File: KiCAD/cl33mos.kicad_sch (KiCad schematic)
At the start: 13 parts, among them J1 USB_B_Micro, J2 Edge2x6_Connector, U2 ESP32-WROOM-32, U3 AMS1117-3.3

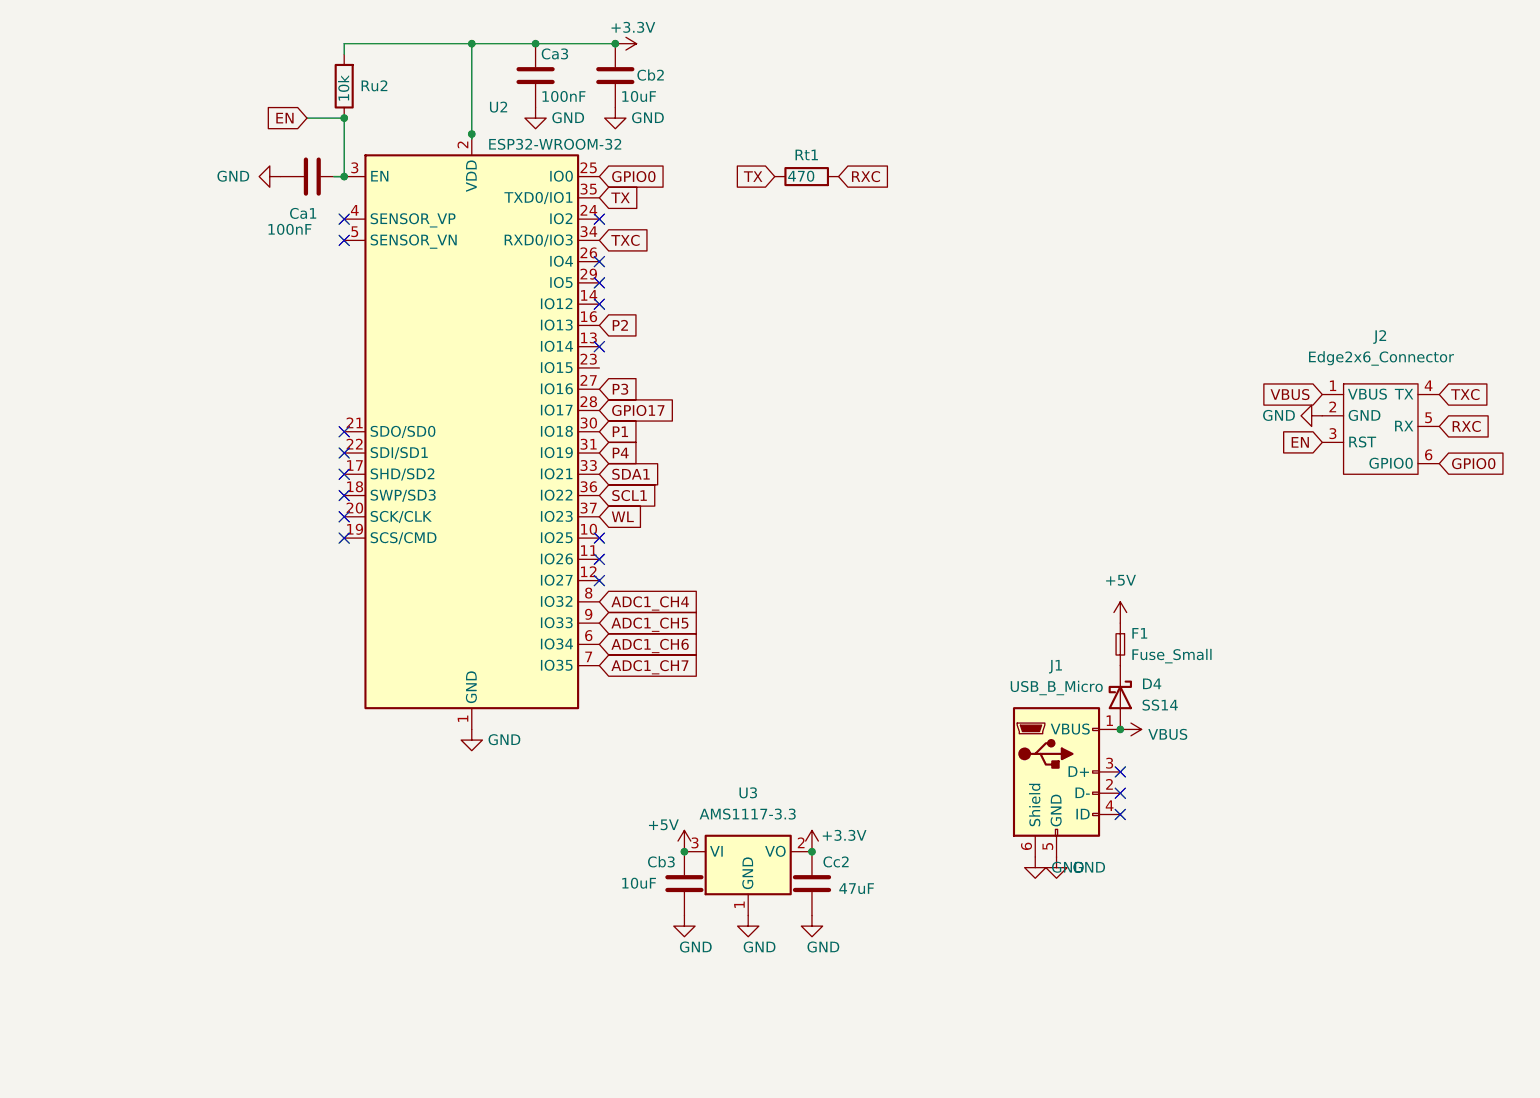
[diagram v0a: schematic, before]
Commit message: Version 1.0.0 (#42)
### Added
- **Hardware Board v2.x & ESP32-S3 Support**: Added PlatformIO configurations (`esp32s3`, `usb_s3`, `wifi_s3`), `BOARD_V20` pin mappings for `ESP32-S3-WROOM-1-N8R2` with USB-C, updated KiCAD schematics/PCB layouts (v2.0–v2.2 with boot/reset push-buttons and improved flyback diode placement), and BOM (`KiCAD/Plant133.csv`).
- **3D-Printed Enclosure & Accessories**:
  - Updated EBox (`scad/box/`) for Board v2.1+ and added OLED support bracket (`OLEDSupport.scad`) and board test fixture (`fixture.scad`).
  - Added reservoir cover/cap (`scad/reservoir_cover/`) with cutouts for the EBox, tubing, and wires.
  - Updated reservoir insert (`scad/reservoir_insert/`) and extracted reusable vitamin models (`vertical_pump.scad`, `float.scad`).
  - Updated solder stencil fixture and added stencil edge-support frame (`scad/stencil_fixture/`).
- **Adafruit IO & SSL/TLS MQTT Support**: Added NTP time synchronization (`og3::Ntp`), SSL/TLS with optional certificate verification, and Adafruit IO MQTT mode with feed filtering/rate-limiting in both firmware and the Svelte MQTT configuration UI.
- **System Status Versioning**: Exposed `software` and `hardware` version fields in `GET /api/status`.
- **Native Unit Tests & Dependabot**: Ported unit tests (`test/test_watering/test_watering.cpp`) to `og3` under `[env:native]`, enabled `pio test -e native` in `util/check.sh`, and added GitHub Actions Dependabot configuration.

### Changed
- **Framework Upgrade**: Upgraded to **og3 v0.7.0**, **og3x-oled v0.6.1**, and **og3x-shtc3 v0.6.0**, linking modules by pointer via `require(...)` and making `DoseLog` an `og3::Module`.
- **Web UI & API Alignment**: Updated Svelte WiFi and MQTT configuration pages to use `og3` variable keys (`essId`, `wifiPassword`, `hostAddr`, `authUser`, `authPassword`) and updated `build-svelte.sh` to use `--etag=always`.
- **MQTT Optimization**: Avoided sending duplicate reservoir status updates per plant.

### Fixed
- **Plant API Validation*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
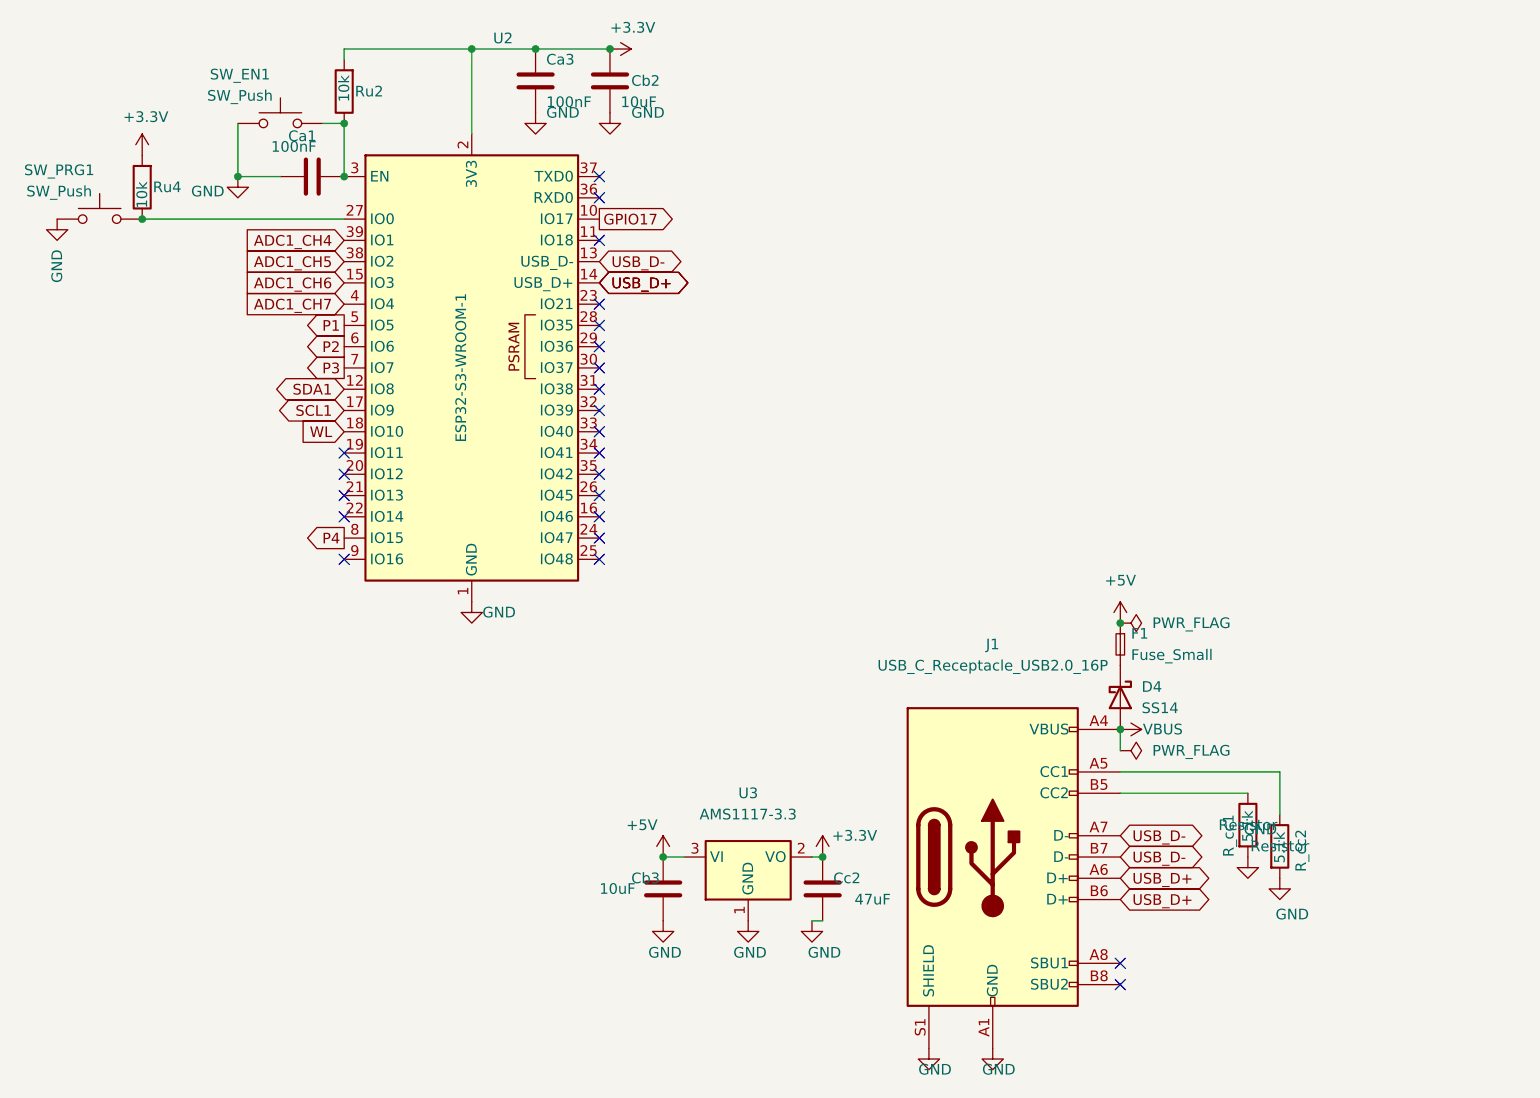
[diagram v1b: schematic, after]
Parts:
- removed J2: Edge2x6_Connector, Library:EdgeConnector_2x3, symbol chl33:Edge2x6_Connector
- removed Rt1: 470, Resistor_SMD:R_0603_1608Metric, symbol Device:R
- added R_cc1, R_cc2: 5.1k, Resistor_SMD:R_0603_1608Metric, symbol Device:R
- added Ru4: 10k, Resistor_SMD:R_0603_1608Metric, symbol Device:R
- added SW_EN1, SW_PRG1: SW_Push, Button_Switch_SMD:SW_SPST_FSMSM, symbol Switch:SW_Push
- J1: value USB_B_Micro -> USB_C_Receptacle_USB2.0_16P; footprint Connector_USB:USB_Micro-B_Amphenol_10118194_Horizontal -> Connector_USB:USB_C_Receptacle_HRO_TYPE-C-31-M-12; symbol Connector:USB_B_Micro -> Connector:USB_C_Receptacle_USB2.0_16P
- U2: value ESP32-WROOM-32 -> ESP32-S3-WROOM-1; footprint RF_Module:ESP32-WROOM-32 -> RF_Module:ESP32-S3-WROOM-1; symbol RF_Module:ESP32-WROOM-32 -> RF_Module:ESP32-S3-WROOM-1
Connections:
- net +3.3V: now also Ru4.2
- net ADC1_CH4: now also U2.39 (IO1); no longer U2.8 (IO32)
- net ADC1_CH5: now also U2.38 (IO2); no longer U2.9 (IO33)
- net ADC1_CH6: now also U2.15 (IO3); no longer U2.6 (IO34)
- net ADC1_CH7: now also U2.4 (IO4); no longer U2.7 (IO35)
- net GND: now also J1.A1 (GND), J1.A12 (GND), J1.B1 (GND), J1.B12 (GND), J1.S1 (SHIELD), U2.40 (GND), U2.41 (GND), R_cc1.2, R_cc2.2, SW_EN1.1, SW_PRG1.1; no longer J1.5 (GND), J1.6 (Shield), U2.15 (GND), U2.38 (GND), U2.39 (GND)
- net GPIO17: now also U2.10 (IO17); no longer U2.28 (IO17)
- net P1: now also U2.5 (IO5); no longer U2.30 (IO18)
- net P2: now also U2.6 (IO6); no longer U2.16 (IO13)
- net P3: now also U2.7 (IO7); no longer U2.27 (IO16)
- net P4: now also U2.8 (IO15); no longer U2.31 (IO19)
- net SCL1: now also U2.17 (IO9); no longer U2.36 (IO22)
- net SDA1: now also U2.12 (IO8); no longer U2.33 (IO21)
- net VBUS: now also J1.A4 (VBUS), J1.A9 (VBUS), J1.B4 (VBUS), J1.B9 (VBUS); no longer J1.1 (VBUS)
- net WL: now also U2.18 (IO10); no longer U2.37 (IO23)
- net USB_D-: now reaches U2.13 (USB_D-)
- net USB_D-: now also J1.A7 (D-), J1.B7 (D-)
- net USB_D+: now reaches U2.14 (USB_D+)
- net USB_D+: now also J1.A6 (D+), J1.B6 (D+)
- net EN: no longer names the net of Ca1.2, Ru2.1, U2.3 (EN)
- net EN: now also SW_EN1.2
- net GPIO0: no longer names the net of U2.25 (IO48)
- net TX: no longer names the net of U2.35 (IO42)
- net TXC: no longer names the net of U2.34 (IO41)
- new net: Ru4.1, SW_PRG1.2, U2.27 (IO0)
- new net: J1.A5 (CC1), R_cc2.1
- new net: J1.B5 (CC2), R_cc1.1
- no-connect marks 19 -> 23
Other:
- moved on the sheet: Ca3, Cb2, Cb3, Cc2, Ru2, U3
